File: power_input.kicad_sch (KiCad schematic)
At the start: 24 parts, among them J1 Barrel_Jack, J201 USBC, U5 TPS630701RNMR

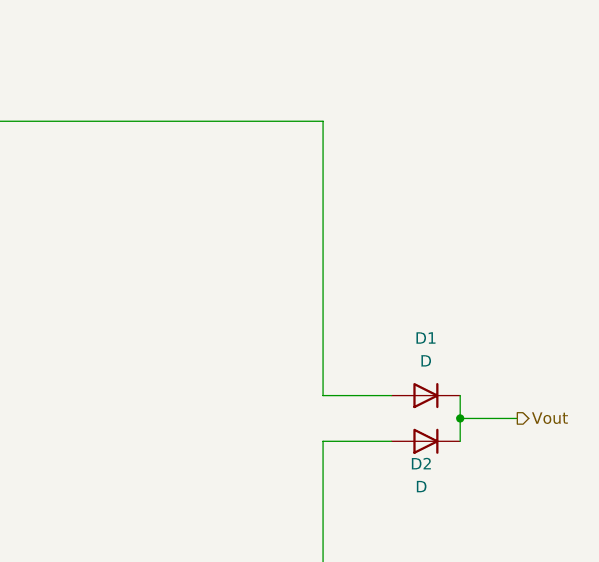
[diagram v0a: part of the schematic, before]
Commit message: Solder jumpers for smaller simpler supply
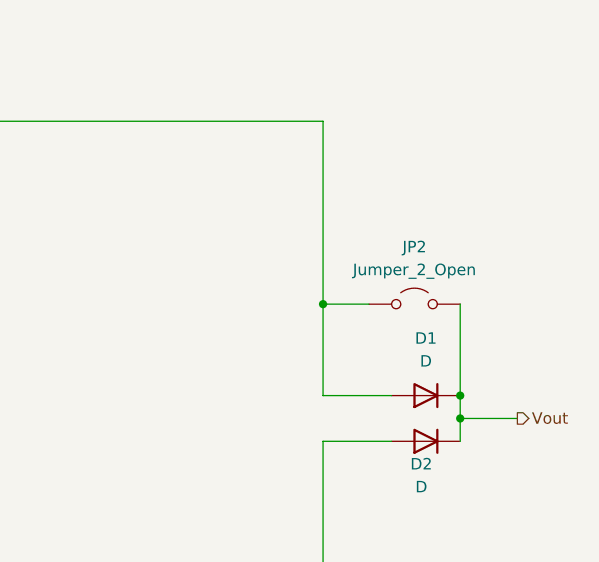
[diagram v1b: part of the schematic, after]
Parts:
- added JP2: Jumper_2_Open, symbol Jumper:Jumper_2_Open
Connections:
- net Vout: now also JP2.2 (B)
- net at D1.2 (A), J201.A9 (VBUS), J201.B9 (VBUS): now also JP2.1 (A)
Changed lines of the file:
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@@
+	)
+	(junction
+		(at 214.63 63.5)
+		(diameter 0)
+		(color 0 0 0 0)
 	)
 	(junction
@@
 	(junction
 		(at 68.58 116.84)
+		(diameter 0)
+		(color 0 0 0 0)
+	)
+	(junction
+		(at 199.39 53.34)
 		(diameter 0)
 		(color 0 0 0 0)
@@
 	(wire
 		(pts
-			(xy 199.39 63.5) (xy 199.39 33.02)
+			(xy 199.39 63.5) (xy 199.39 53.34)
 		)
 		(stroke
@@
 	(wire
 		(pts
+			(xy 199.39 53.34) (xy 199.39 33.02)
+		)
+		(stroke
+			(width 0)
+			(type default)
+		)
+	)
+	(wire
+		(pts
 			(xy 154.94 106.68) (xy 162.56 106.68)
 		)
@@
 	(wire
 		(pts
+			(xy 199.39 53.34) (xy 204.47 53.34)
+		)
+		(stroke
+			(width 0)
+			(type default)
+		)
+	)
+	(wire
+		(pts
 			(xy 68.58 119.38) (xy 68.58 116.84)
 		)
@@
 		(pts
 			(xy 124.46 87.63) (xy 124.46 101.6)
+		)
+		(stroke
+			(width 0)
+			(type default)
+		)
+	)
+	(wire
+		(pts
+			(xy 214.63 53.34) (xy 214.63 63.5)
 		)
 		(stroke
@@
 					(unit 1)
 				)
+			)
+		)
+	)
+	(symbol
+		(lib_id "Jumper:Jumper_2_Open")
+		(at 209.55 53.34 0)
+		(unit 1)
+		(exclude_from_sim no)
+		(in_bom yes)
+		(on_board yes)
+		(dnp no)
+		(fields_autoplaced yes)
+		(property "Reference" "JP2"
+			(at 209.55 46.99 0)
+			(effects
+				(font
+					(size 1.27 1.27)
+				)
+			)
+		)
+		(property "Value" "Jumper_2_Open"
+			(at 209.55 49.53 0)
+			(effects
+				(font
+					(size 1.27 1.27)
+				)
+			)
+		)
+		(property "Footprint" ""
+			(at 209.55 53.34 0)
+			(effects
+				(font
+					(size 1.27 1.27)
+				)
+				(hide yes)
+			)
+		)
+		(property "Datasheet" "~"
+			(at 209.55 53.34 0)
+			(effects
+				(font
+					(size 1.27 1.27)
+				)
+				(hide yes)
+			)
+		)
+		(property "Description" "Jumper, 2-pole, open"
+			(at 209.55 53.34 0)
+			(effects
+				(font
+					(size 1.27 1.27)
+				)
+				(hide yes)
+			)
+		)
+		(pin "2"
+		)
+		(pin "1"
+		)
+		(instances
+			(project ""
+				(path "/3f1ccd97-6ac6-4e7a-a00a-840cd07719d8/60b998c9-c5a3-404e-89bd-843282e77358"
+					(reference "JP2")
+					(unit 1)
+				)

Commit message: Part selection
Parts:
- removed D1, D2: D, symbol Device:D
- removed J1: Barrel_Jack, symbol Connector:Barrel_Jack
- removed JP2: Jumper_2_Open, symbol Jumper:Jumper_2_Open
- added D201, D202: SS14, Diode_SMD:D_SMA_Handsoldering, symbol Device:D
- added J201: Barrel_Jack_MountingPin, Connector_BarrelJack:BarrelJack_GCT_DCJ200-10-A_Horizontal, symbol Connector:Barrel_Jack_MountingPin
- added JP201: SolderJumper_2_Open, Jumper:SolderJumper-2_P1.3mm_Open_RoundedPad1.0x1.5mm, symbol Jumper:SolderJumper_2_Open
- C201: renamed from C215; now left out of the parts list
- C202: renamed from C216; now left out of the parts list
- C203: renamed from C217; footprint Capacitor_SMD:C_1206_3216Metric_Pad1.33x1.80mm_HandSolder -> Capacitor_SMD:C_0805_2012Metric_Pad1.18x1.45mm_HandSolder; LCSC (none) -> C7393927
- C204: renamed from C218; now left out of the parts list
- C205: renamed from C213; now left out of the parts list
- C206: renamed from C214; now left out of the parts list
- C207: renamed from C219; now left out of the parts list
- J202: renamed from J201; LCSC (none) -> C42400234
- L201: renamed from L202; footprint Inductor_SMD_Wurth:L_Wurth_WE-LQSH-2512 -> Inductor_SMD:L_Cenker_CKCS4020; LCSC (none) -> C5442006
- R201: renamed from R223; now left out of the parts list
- R202: renamed from R212; now left out of the parts list
- R203: renamed from R201; now left out of the parts list
- R204: renamed from R228; footprint Resistor_SMD:R_1206_3216Metric_Pad1.30x1.75mm_HandSolder -> Resistor_SMD:R_0805_2012Metric_Pad1.20x1.40mm_HandSolder; LCSC (none) -> C5140137
- R205: renamed from R227; footprint Resistor_SMD:R_1206_3216Metric_Pad1.30x1.75mm_HandSolder -> Resistor_SMD:R_0805_2012Metric_Pad1.20x1.40mm_HandSolder; LCSC (none) -> C3016836
- R206: renamed from R229; footprint Resistor_SMD:R_1206_3216Metric_Pad1.30x1.75mm_HandSolder -> Resistor_SMD:R_0805_2012Metric_Pad1.20x1.40mm_HandSolder; LCSC (none) -> C365243
- R207: renamed from R211; now left out of the parts list
- R208: renamed from R202; now left out of the parts list
- R209: renamed from R222; now left out of the parts list
- TP201: renamed from TP5; footprint TestPoint:TestPoint_Pad_D1.0mm -> TestPoint:TestPoint_Pad_D2.0mm; now left out of the parts list
- TP202: renamed from TP4; footprint TestPoint:TestPoint_Pad_D1.0mm -> TestPoint:TestPoint_Pad_D2.0mm; now left out of the parts list
- U201: renamed from U5; LCSC (none) -> C109322
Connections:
- net GND: now also J201.2
- net Vout: now also D201.1 (K), D202.1 (K), JP201.2 (B)
- net at C201.1, C202.1, C203.1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: now also J201.1
- net at C205.1, C206.1, C207.1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: now also D202.2 (A)
- net at J202.A9 (VBUS), J202.B9 (VBUS): now also D201.2 (A), JP201.1 (A)
- no-connect marks 1 -> 2

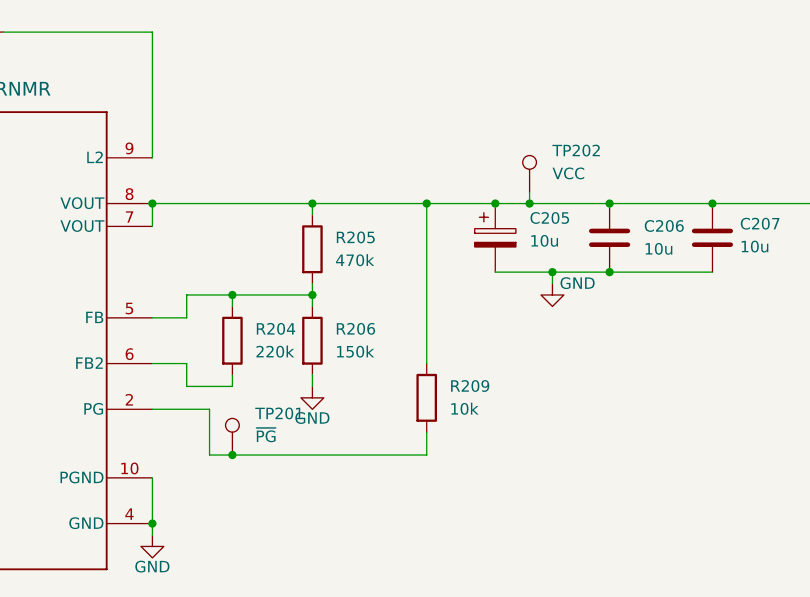
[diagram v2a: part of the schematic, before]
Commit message: Add more LEDs
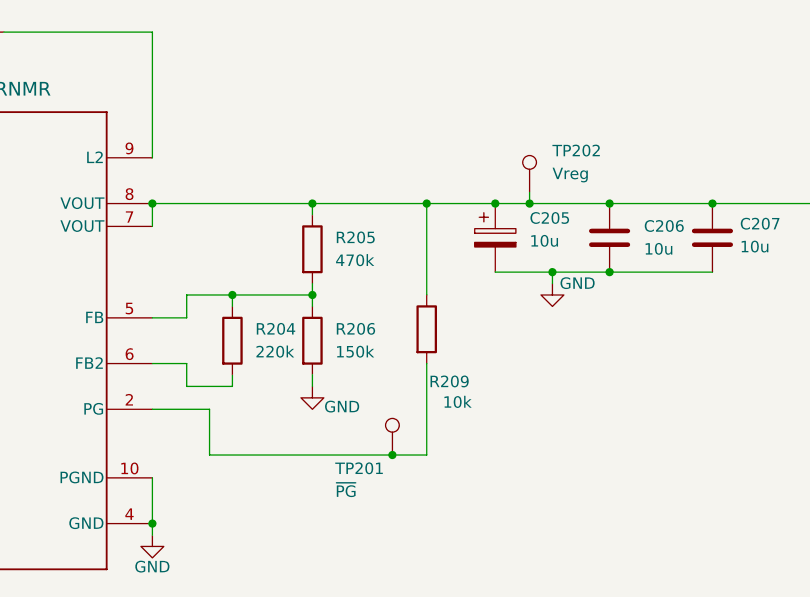
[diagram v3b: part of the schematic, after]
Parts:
- TP202: value VCC -> Vreg
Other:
- moved on the sheet: TP201

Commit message: Connection naming
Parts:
- J201: value Barrel_Jack_MountingPin -> DC In
- JP201: value SolderJumper_2_Open -> USB Only
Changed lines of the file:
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@@
 			)
 		)
-		(property "Value" "Barrel_Jack_MountingPin"
+		(property "Value" "DC In"
 			(at 29.21 102.87 0)
 			(effects
@@
 			)
 		)
-		(property "Value" "SolderJumper_2_Open"
+		(property "Value" "USB Only"
 			(at 209.55 49.53 0)
 			(effects

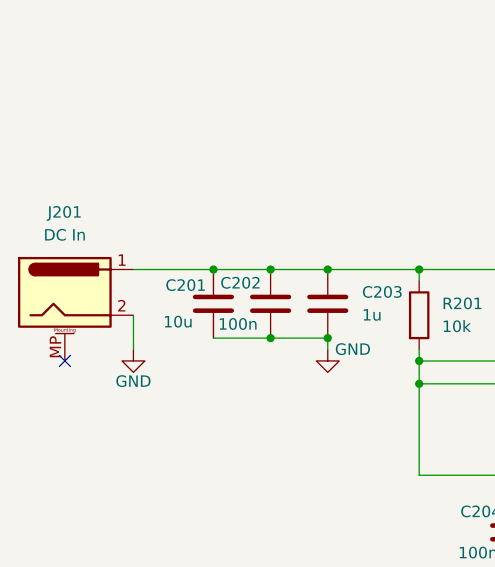
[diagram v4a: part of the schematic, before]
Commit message: Swap out barrel jack
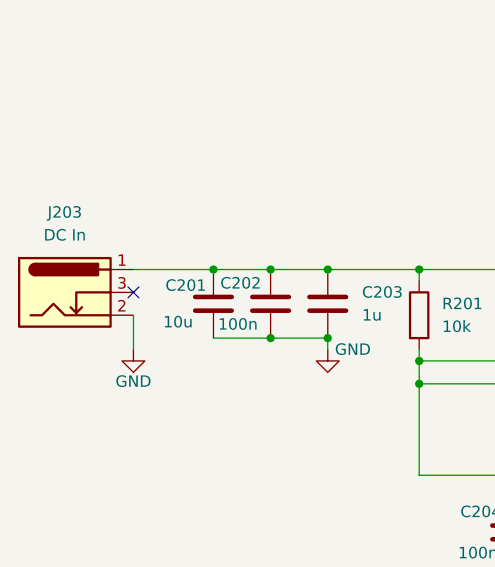
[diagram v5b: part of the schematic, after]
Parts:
- removed J201: DC In, Connector_BarrelJack:BarrelJack_GCT_DCJ200-10-A_Horizontal, symbol Connector:Barrel_Jack_MountingPin
- added J203: DC In, Connector_BarrelJack:BarrelJack_Horizontal, symbol Connector:Barrel_Jack_Switch
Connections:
- net GND: now also J203.2
- net at C201.1, C202.1, C203.1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: now also J203.1
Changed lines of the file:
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@@
 	)
 	(no_connect
-		(at 29.21 116.84)
+		(at 36.83 109.22)
 	)
 	(no_connect
@@
 	)
 	(symbol
-		(lib_id "Connector:Barrel_Jack_MountingPin")
-		(at 29.21 109.22 0)
-		(unit 1)
-		(exclude_from_sim no)
-		(in_bom no)
-		(on_board yes)
-		(dnp no)
-		(fields_autoplaced yes)
-		(property "Reference" "J201"
-			(at 29.21 100.33 0)
-			(effects
-				(font
-					(size 1.27 1.27)
-				)
-			)
-		)
-		(property "Value" "DC In"
-			(at 29.21 102.87 0)
-			(effects
-				(font
-					(size 1.27 1.27)
-				)
-			)
-		)
-		(property "Footprint" "Connector_BarrelJack:BarrelJack_GCT_DCJ200-10-A_Horizontal"
-			(at 30.48 110.236 0)
-			(effects
-				(font
-					(size 1.27 1.27)
-				)
-				(hide yes)
-			)
-		)
-		(property "Datasheet" "~"
-			(at 30.48 110.236 0)
-			(effects
-				(font
-					(size 1.27 1.27)
-				)
-				(hide yes)
-			)
-		)
-		(property "Description" "DC Barrel Jack with a mounting pin"
-			(at 29.21 109.22 0)
-			(effects
-				(font
-					(size 1.27 1.27)
-				)
-				(hide yes)
-			)
-		)
-		(pin "1"
-		)
-		(pin "MP"
-		)
-		(pin "2"
-		)
-		(instances
-			(project ""
-				(path "/3f1ccd97-6ac6-4e7a-a00a-840cd07719d8/60b998c9-c5a3-404e-89bd-843282e77358"
-					(reference "J201")
-					(unit 1)
-				)
-			)
-		)
-	)
-	(symbol
 		(lib_id "power:GND")
 		(at 142.24 127 0)
@@
 					(unit 1)
 				)
+			)
+		)
+	)
+	(symbol
+		(lib_id "Connector:Barrel_Jack_Switch")
+		(at 29.21 109.22 0)
+		(unit 1)
+		(exclude_from_sim no)
+		(in_bom yes)
+		(on_board yes)
+		(dnp no)
+		(fields_autoplaced yes)
+		(property "Reference" "J203"
+			(at 29.21 100.33 0)
+			(effects
+				(font
+					(size 1.27 1.27)
+				)
+			)
+		)
+		(property "Value" "DC In"
+			(at 29.21 102.87 0)
+			(effects
+				(font
+					(size 1.27 1.27)
+				)
+			)
+		)
+		(property "Footprint" "Connector_BarrelJack:BarrelJack_Horizontal"
+			(at 30.48 110.236 0)
+			(effects
+				(font
+					(size 1.27 1.27)
+				)
+				(hide yes)
+			)
+		)
+		(property "Datasheet" "~"
+			(at 30.48 110.236 0)
+			(effects
+				(font
+					(size 1.27 1.27)
+				)
+				(hide yes)
+			)
+		)
+		(property "Description" "DC Barrel Jack with an internal switch"
+			(at 29.21 109.22 0)
+			(effects
+				(font
+					(size 1.27 1.27)
+				)
+				(hide yes)
+			)
+		)
+		(pin "2"
+		)
+		(pin "3"
+		)
+		(pin "1"
+		)
+		(instances
+			(project ""
+				(path "/3f1ccd97-6ac6-4e7a-a00a-840cd07719d8/60b998c9-c5a3-404e-89bd-843282e77358"
+					(reference "J203")
+					(unit 1)
+				)

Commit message: Update BOM options for export
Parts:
- J203: now left out of the parts list
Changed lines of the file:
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@@
 		(unit 1)
 		(exclude_from_sim no)
-		(in_bom yes)
+		(in_bom no)
 		(on_board yes)
 		(dnp no)
